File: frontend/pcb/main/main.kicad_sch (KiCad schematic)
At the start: 56 parts, among them J1 Ext, J2 CONN_01X02, J3 Conn_01x09, J4 Debug, J5 RS485, J6 Conn_01x04, J7 Conn_01x02, J8 Conn_01x02, J9 Conn_01x02, K1 G6B-1114C-US5DC, Q1 MMBT3904, Q2 MMBT3904, Q3 BSS138, SW1 SW_SPST, SW2 SW_SPST, U1 ESP32-WROOM-32, U2 AP1117-33, U3 MAX485E, U4 DSN-MINI-360

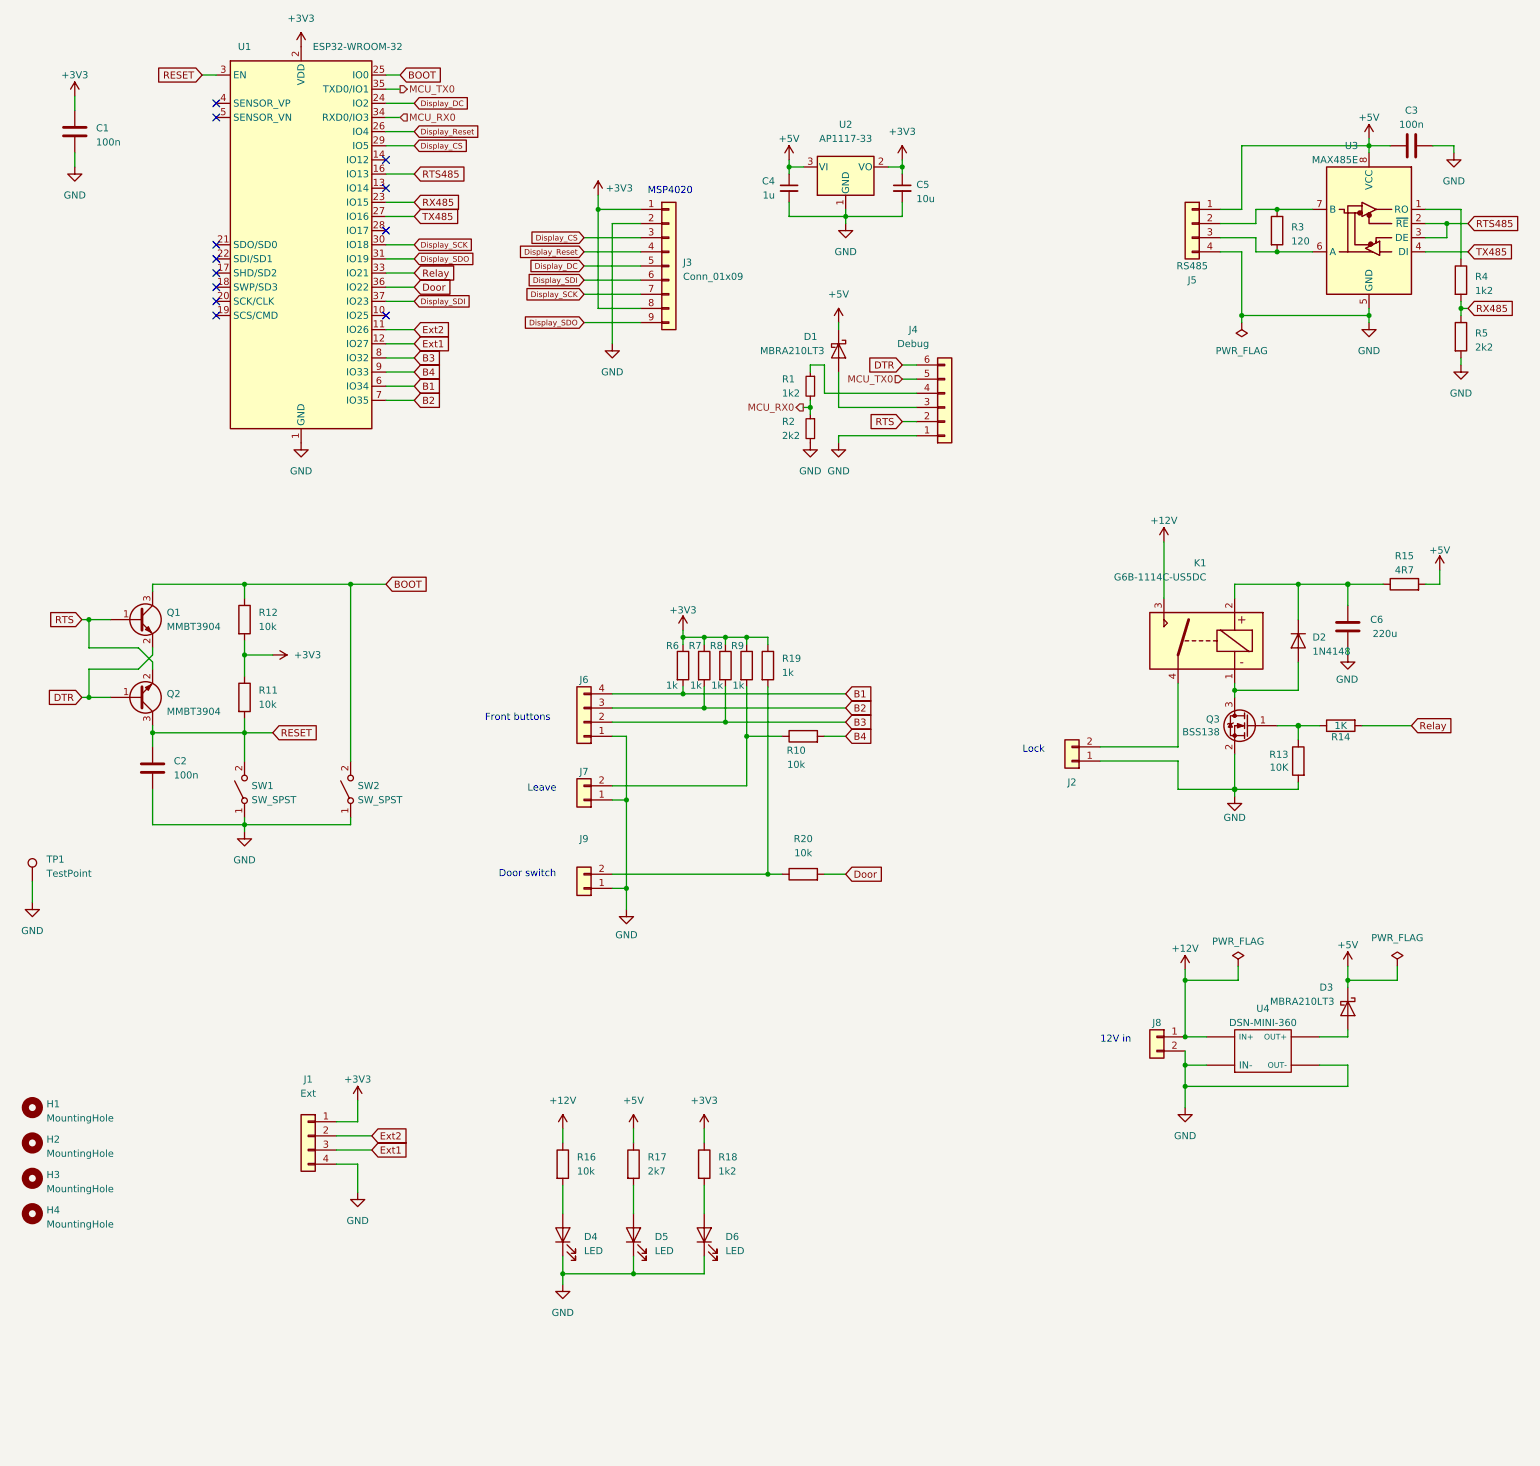
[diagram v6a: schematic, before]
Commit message: Add seconds display connector.
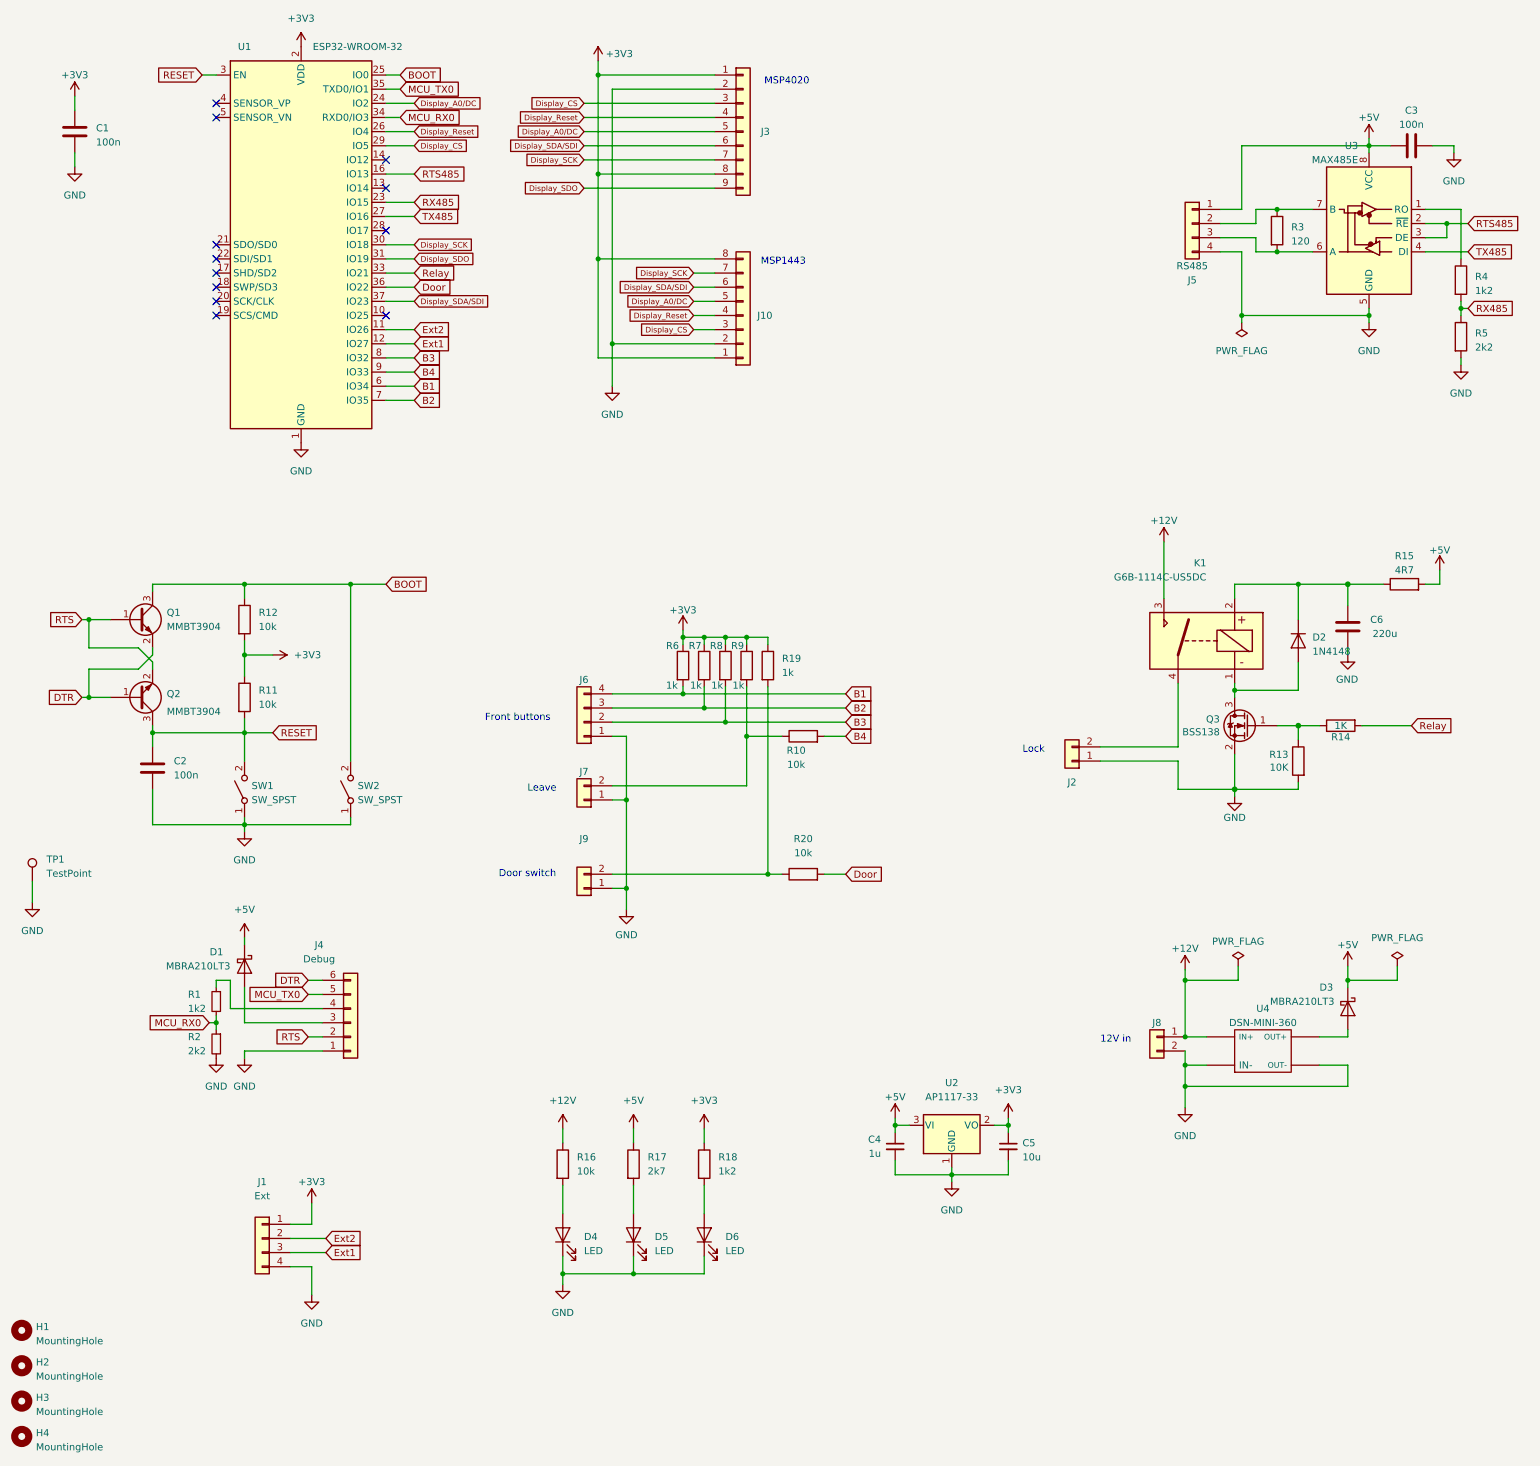
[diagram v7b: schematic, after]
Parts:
- added J10: Display1443, Connector_PinHeader_2.54mm:PinHeader_1x08_P2.54mm_Vertical, symbol Connector_Generic:Conn_01x08
- J3: value Conn_01x09 -> Display4020
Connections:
- net +3V3: now also J10.1 (Pin_1), J10.8 (Pin_8)
- net Display_CS: now also J10.3 (Pin_3)
- net Display_Reset: now also J10.4 (Pin_4)
- net Display_SCK: now also J10.7 (Pin_7)
- net GND: now also J10.2 (Pin_2)
- net Display_DC renamed Display_A0/DC
- net Display_A0/DC: now also J10.5 (Pin_5)
- net Display_SDI renamed Display_SDA/SDI
- net Display_SDA/SDI: now also J10.6 (Pin_6)
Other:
- note added: "MSP1443"
- moved on the sheet: C4, C5, D1, H1, H2, H3, H4, J1, J3, J4, R1, R2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

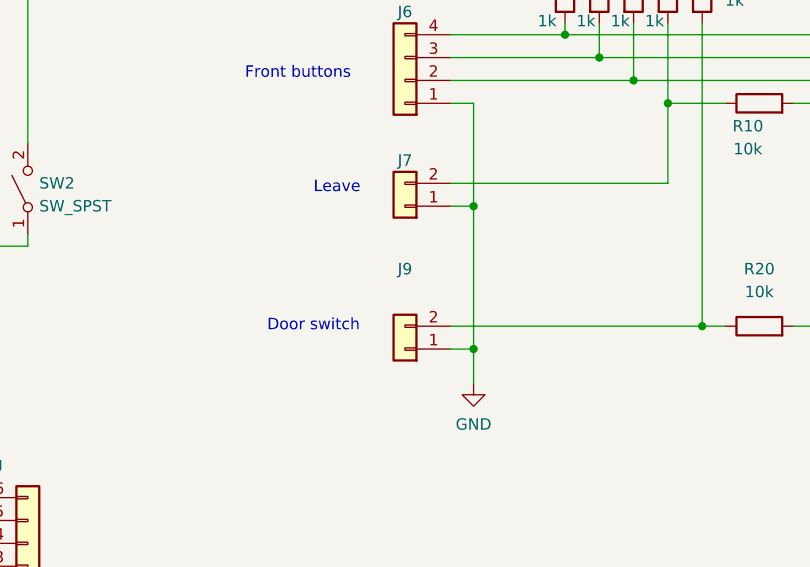
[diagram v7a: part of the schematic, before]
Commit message: Start placing additional components.
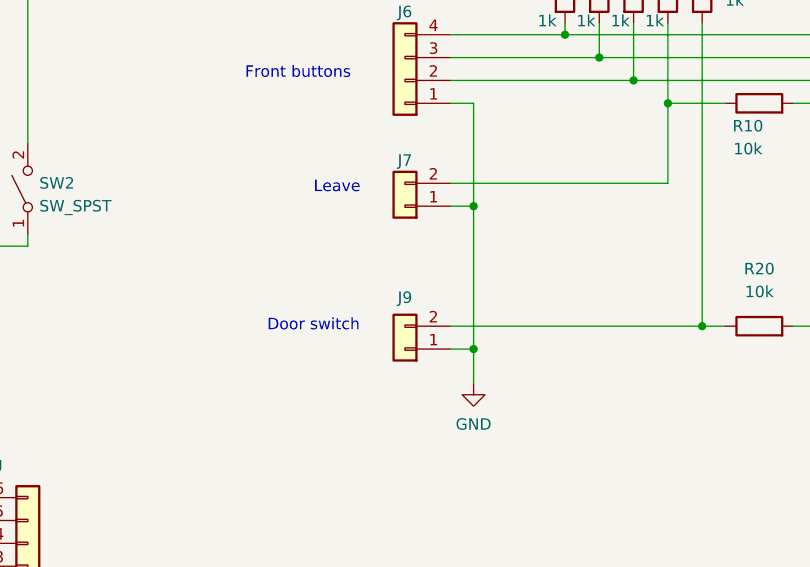
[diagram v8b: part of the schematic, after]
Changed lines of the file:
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@@
   )
   (symbol (lib_id "Connector_Generic:Conn_01x02") (at 124.46 175.26 180) (unit 1)
-    (exclude_from_sim no) (in_bom yes) (on_board yes) (dnp no) (fields_autoplaced)
-    (property "Reference" "J9" (at 124.46 166.37 0)
+    (exclude_from_sim no) (in_bom yes) (on_board yes) (dnp no)
+    (property "Reference" "J9" (at 124.46 169.545 0)
       (effects (font (size 1.27 1.27)))
     )
